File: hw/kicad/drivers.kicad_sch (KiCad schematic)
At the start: 81 parts

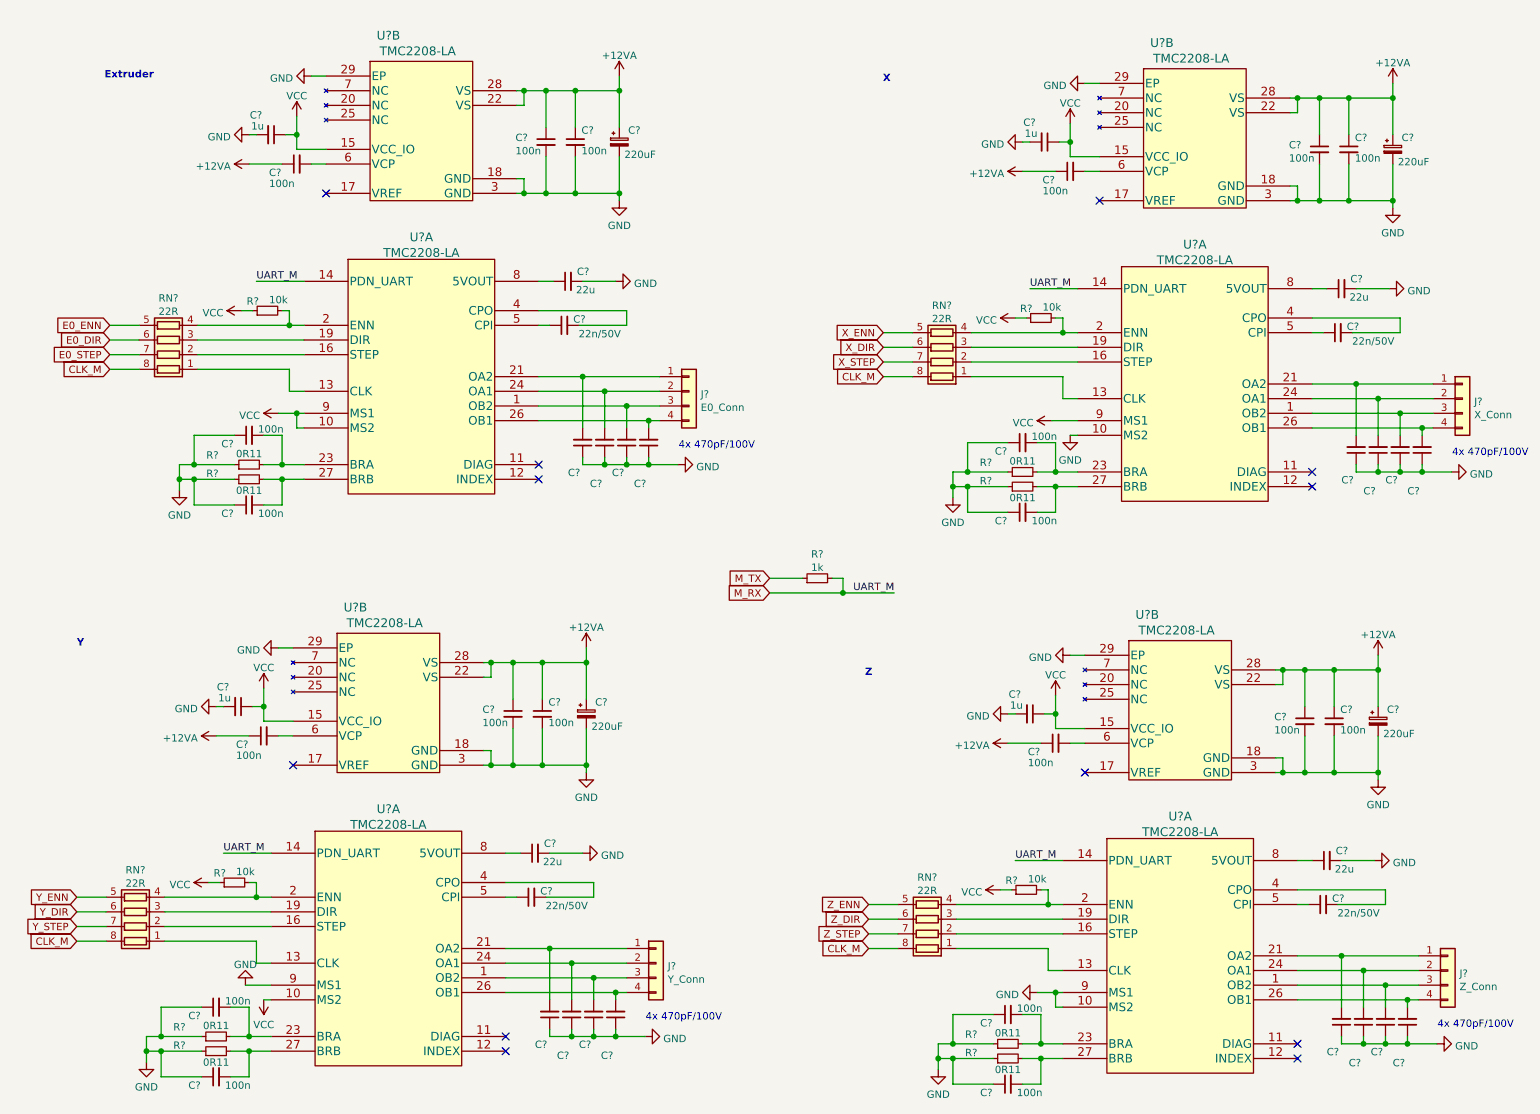
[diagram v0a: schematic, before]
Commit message: fix - broken drivers.kicad_sch
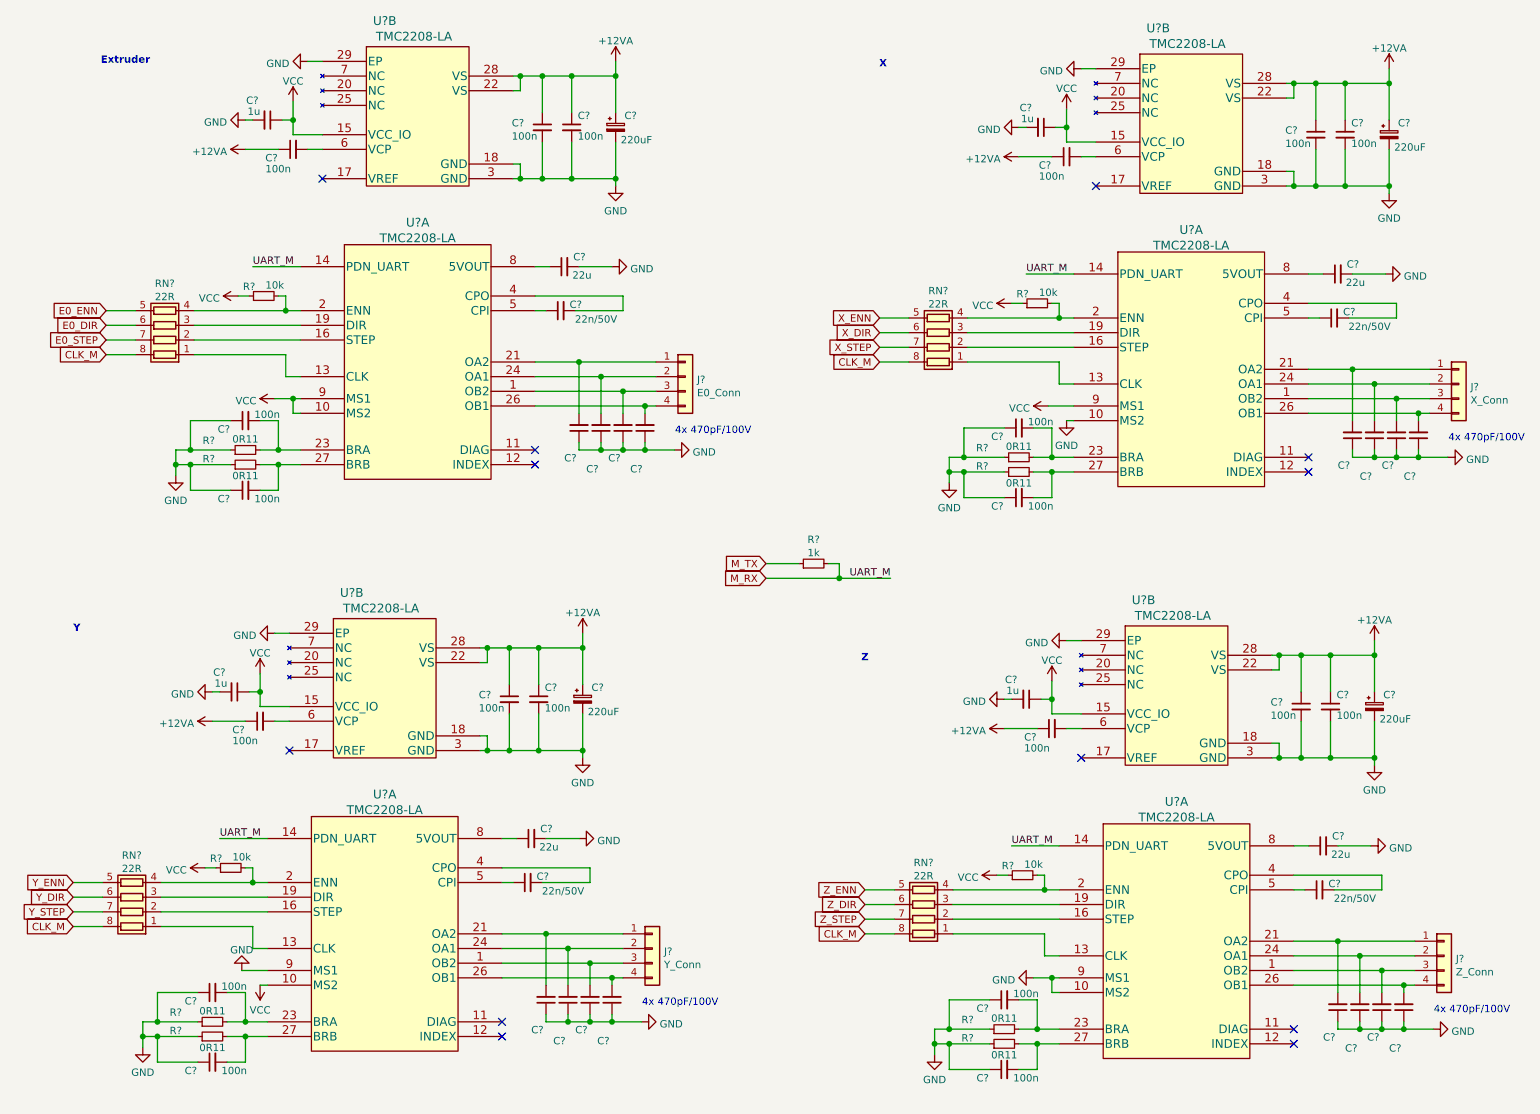
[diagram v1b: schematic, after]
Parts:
- removed C? (x20): 100n, symbol Device:C_Small
- removed C? (x4): 220uF, symbol Device:C_Polarized_Small
- removed C? (x16): 470p, symbol Device:C_Small
- removed C? (x4): 22u, symbol Device:C_Small
- removed C? (x4): 1u, symbol Device:C_Small
- removed C? (x4): 22n/50V, symbol Device:C_Small
- removed J?: Z_Conn, symbol Connector_Generic:Conn_01x04
- removed J?: E0_Conn, symbol Connector_Generic:Conn_01x04
- removed J?: X_Conn, symbol Connector_Generic:Conn_01x04
- removed J?: Y_Conn, symbol Connector_Generic:Conn_01x04
- removed R? (x4): 10k, symbol Device:R_Small
- removed R?: 1k, symbol Device:R_Small
- removed R? (x8): 0R11, symbol Device:R_Small
- removed RN? (x4): 22R, Resistor_SMD:R_Array_Concave_4x0603, symbol Device:R_Pack04
- removed U? (x8): TMC2208-LA, Package_DFN_QFN:QFN-28-1EP_5x5mm_P0.5mm_EP3.35x3.35mm, symbol Kamtar:TMC2208-LA
- added C? (x16): 470p, symbol Device:C_Small
- added C? (x20): 100n, symbol Device:C_Small
- added C? (x4): 1u, symbol Device:C_Small
- added C? (x4): 22n/50V, symbol Device:C_Small
- added C? (x4): 220uF, symbol Device:C_Polarized_Small
- added C? (x4): 22u, symbol Device:C_Small
- added J?: E0_Conn, symbol Connector_Generic:Conn_01x04
- added J?: Y_Conn, symbol Connector_Generic:Conn_01x04
- added J?: X_Conn, symbol Connector_Generic:Conn_01x04
- added J?: Z_Conn, symbol Connector_Generic:Conn_01x04
- added R? (x8): 0R11, symbol Device:R_Small
- added R? (x4): 10k, symbol Device:R_Small
- added R?: 1k, symbol Device:R_Small
- added RN? (x4): 22R, Resistor_SMD:R_Array_Concave_4x0603, symbol Device:R_Pack04
- added U? (x8): TMC2208-LA, Package_DFN_QFN:QFN-28-1EP_5x5mm_P0.5mm_EP3.35x3.35mm, symbol Kamtar:TMC2208-LA
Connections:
- net +12VA: now also C?.1, C?.1, C?.1, C?.1, C?.1, C?.1, C?.1, C?.1, C?.1, C?.1, C?.1, C?.1, C?.1, C?.1, C?.1, C?.1, U?.22 (VS), U?.22 (VS), U?.22 (VS), U?.22 (VS), U?.28 (VS), U?.28 (VS), U?.28 (VS), U?.28 (VS)
- net CLK_M: now also RN?.8 (R1.2), RN?.8 (R1.2), RN?.8 (R1.2), RN?.8 (R1.2)
- net E0_DIR: now also RN?.6 (R3.2)
- net E0_ENN: now also RN?.5 (R4.2)
- net E0_STEP: now also RN?.7 (R2.2)
- net GND: now also C?.1, C?.1, C?.1, C?.1, C?.1, C?.1, C?.1, C?.1, C?.1, C?.1, C?.1, C?.1, C?.1, C?.1, C?.1, C?.1, C?.1, C?.1, C?.1, C?.1, C?.1, C?.1, C?.1, C?.1, C?.2, C?.2, C?.2, C?.2, C?.2, C?.2, C?.2, C?.2, C?.2, C?.2, C?.2, C?.2, C?.2, C?.2, C?.2, C?.2, C?.2, C?.2, C?.2, C?.2, R?.1, R?.1, R?.1, R?.1, R?.1, R?.1, R?.1, R?.1, U?.10 (MS2), U?.10 (MS2), U?.18 (GND), U?.18 (GND), U?.18 (GND), U?.18 (GND), U?.29 (EP), U?.29 (EP), U?.29 (EP), U?.29 (EP), U?.3 (GND), U?.3 (GND), U?.3 (GND), U?.3 (GND), U?.9 (MS1), U?.9 (MS1)
- net M_RX: now also R?.2, U?.14 (PDN_UART), U?.14 (PDN_UART), U?.14 (PDN_UART), U?.14 (PDN_UART)
- net M_TX: now also R?.1
- net VCC: now also C?.1, C?.1, C?.1, C?.1, R?.1, R?.1, R?.1, R?.1, U?.10 (MS2), U?.10 (MS2), U?.15 (VCC_IO), U?.15 (VCC_IO), U?.15 (VCC_IO), U?.15 (VCC_IO), U?.9 (MS1), U?.9 (MS1)
- net X_DIR: now also RN?.6 (R3.2)
- net X_ENN: now also RN?.5 (R4.2)
- net X_STEP: now also RN?.7 (R2.2)
- net Y_DIR: now also RN?.6 (R3.2)
- net Y_ENN: now also RN?.5 (R4.2)
- net Y_STEP: now also RN?.7 (R2.2)
- net Z_DIR: now also RN?.6 (R3.2)
- net Z_ENN: now also RN?.5 (R4.2)
- net Z_STEP: now also RN?.7 (R2.2)
- new net: C?.2, J?.1 (Pin_1), U?.21 (OA2) (x4)
- new net: C?.2, R?.2, U?.23 (BRA) (x4)
- new net: C?.2, R?.2, U?.27 (BRB) (x4)
- new net: C?.2, J?.2 (Pin_2), U?.24 (OA1) (x4)
- new net: C?.2, J?.3 (Pin_3), U?.1 (OB2) (x4)
- new net: C?.2, J?.4 (Pin_4), U?.26 (OB1) (x4)
- new net: C?.1, U?.5 (CPI) (x4)
- new net: C?.2, U?.4 (CPO) (x4)
- new net: C?.2, U?.6 (VCP) (x4)
- new net: RN?.1 (R1.1), U?.13 (CLK) (x4)
- new net: RN?.2 (R2.1), U?.16 (STEP) (x4)
- new net: RN?.3 (R3.1), U?.19 (DIR) (x4)
- new net: R?.2, RN?.4 (R4.1), U?.2 (ENN) (x4)
- new net: C?.1, U?.8 (5VOUT) (x4)

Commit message: reannotated
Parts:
- added TP1, TP2, TP3, TP4: TestPoint, symbol Connector:TestPoint
- gave numbers to parts that had none: 77
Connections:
- net at U6.11 (DIAG): now also TP1.1
- net at U8.11 (DIAG): now also TP3.1
- net at U9.11 (DIAG): now also TP4.1
- net at U7.11 (DIAG): now also TP2.1
- no-connect marks 12 -> 8

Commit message: hw schematics
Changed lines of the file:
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@@
   (symbol (lib_id "Device:C_Small") (at 95.885 160.02 90) (unit 1)
     (in_bom yes) (on_board yes)
-    (property "Reference" "C59" (id 0) (at 99.5691 158.9658 90)
+    (property "Reference" "C59" (id 0) (at 100.8391 158.9658 90)
       (effects (font (size 1.27 1.27)) (justify left))
     )
@@
   (symbol (lib_id "Device:C_Small") (at 96.52 152.4 90) (unit 1)
     (in_bom yes) (on_board yes)
-    (property "Reference" "C57" (id 0) (at 100.2041 150.7108 90)
+    (property "Reference" "C57" (id 0) (at 101.4741 150.7108 90)
       (effects (font (size 1.27 1.27)) (justify left))
     )
@@
   (symbol (lib_id "Device:C_Small") (at 101.6 60.96 90) (unit 1)
     (in_bom yes) (on_board yes)
-    (property "Reference" "C33" (id 0) (at 105.2841 59.9058 90)
+    (property "Reference" "C33" (id 0) (at 106.5541 59.9058 90)
       (effects (font (size 1.27 1.27)) (justify left))
     )
@@
   (symbol (lib_id "Device:C_Small") (at 102.235 53.34 90) (unit 1)
     (in_bom yes) (on_board yes)
-    (property "Reference" "C31" (id 0) (at 105.9191 51.6508 90)
+    (property "Reference" "C31" (id 0) (at 107.1891 51.6508 90)
       (effects (font (size 1.27 1.27)) (justify left))
     )
@@
   (symbol (lib_id "Device:C_Small") (at 233.045 161.29 90) (unit 1)
     (in_bom yes) (on_board yes)
-    (property "Reference" "C60" (id 0) (at 236.7291 160.2358 90)
+    (property "Reference" "C60" (id 0) (at 237.9991 160.2358 90)
       (effects (font (size 1.27 1.27)) (justify left))
     )
@@
   (symbol (lib_id "Device:C_Small") (at 233.68 153.67 90) (unit 1)
     (in_bom yes) (on_board yes)
-    (property "Reference" "C58" (id 0) (at 237.3641 151.9808 90)
+    (property "Reference" "C58" (id 0) (at 238.6341 151.9808 90)
       (effects (font (size 1.27 1.27)) (justify left))
     )
@@
   (symbol (lib_id "Device:C_Small") (at 235.585 62.23 90) (unit 1)
     (in_bom yes) (on_board yes)
-    (property "Reference" "C34" (id 0) (at 239.2691 61.1758 90)
+    (property "Reference" "C34" (id 0) (at 240.5391 61.1758 90)
       (effects (font (size 1.27 1.27)) (justify left))
     )
@@
   (symbol (lib_id "Device:C_Small") (at 236.22 54.61 90) (unit 1)
     (in_bom yes) (on_board yes)
-    (property "Reference" "C32" (id 0) (at 239.9041 52.9208 90)
-      (effects (font (size 1.27 1.27)) (justify left))
-    )
+    (property "Reference" "C32" (id 0) (at 241.1741 52.9208 90)
+      (effects (font (size 1.27 1.27)) (justify left))
+    )
